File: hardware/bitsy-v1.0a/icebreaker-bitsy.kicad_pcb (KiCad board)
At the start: 4 copper layers, 35.6 x 17.8 mm, 93 parts, among them J1 3V3, J10 4, J11 1, J12 5, J13 7, J14 6, J15 16, J16 15, J17 18, J18 17, J19 19, J2 3V3, J20 20, J21 21, J22 22, J23 23, J24 8, J25 9, J26 13, J27 14, J28 12, J29 11, J3 VIN, J30 10, J31 CDONE, J32 CRESET, J33 USB_C, J34 PROG, J4 GND, J5 GND, J6 GND, J7 2, J8 3, J9 0, P1 UP, P2 UP, P3 UP, P4 UP, SW1 TACT, U1 USBLC6-2, U2 TLV75512PDRV, U3 TLV75533PDRV, U4 LY68L6400, U5 W25Q, U6 ICE40UP5K-SG48, X1 12MHz

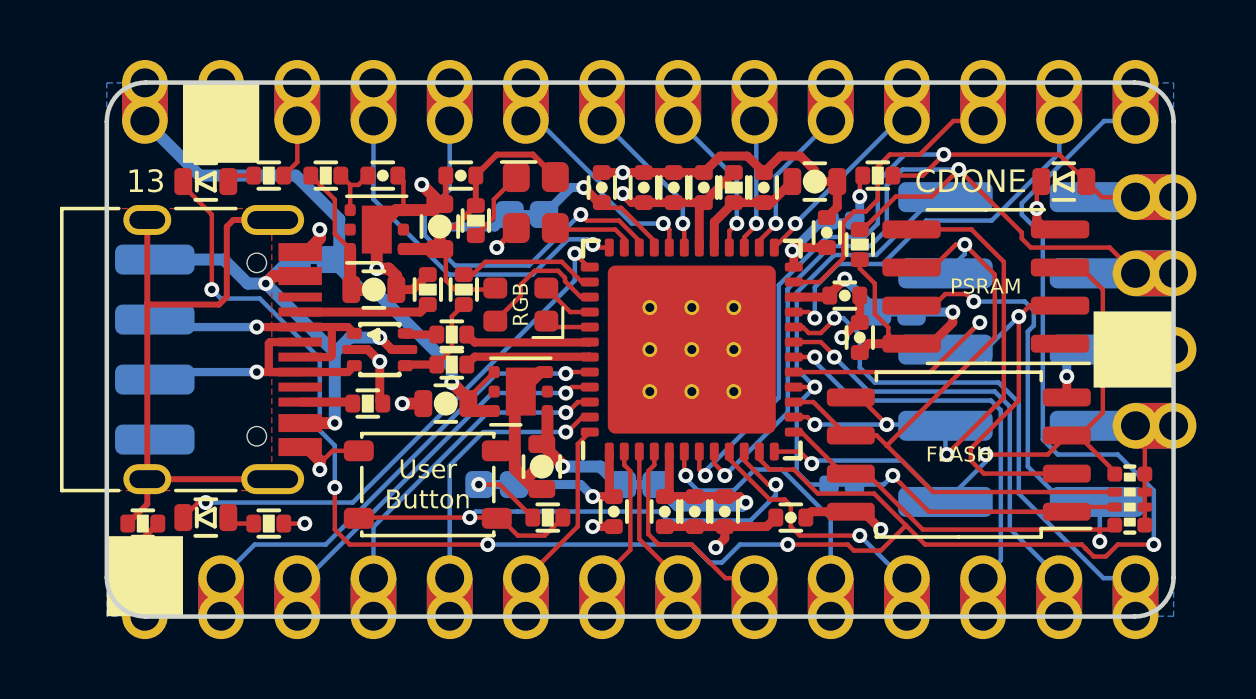
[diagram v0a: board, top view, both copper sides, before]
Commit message: Finish routing bitsy-v1.0a
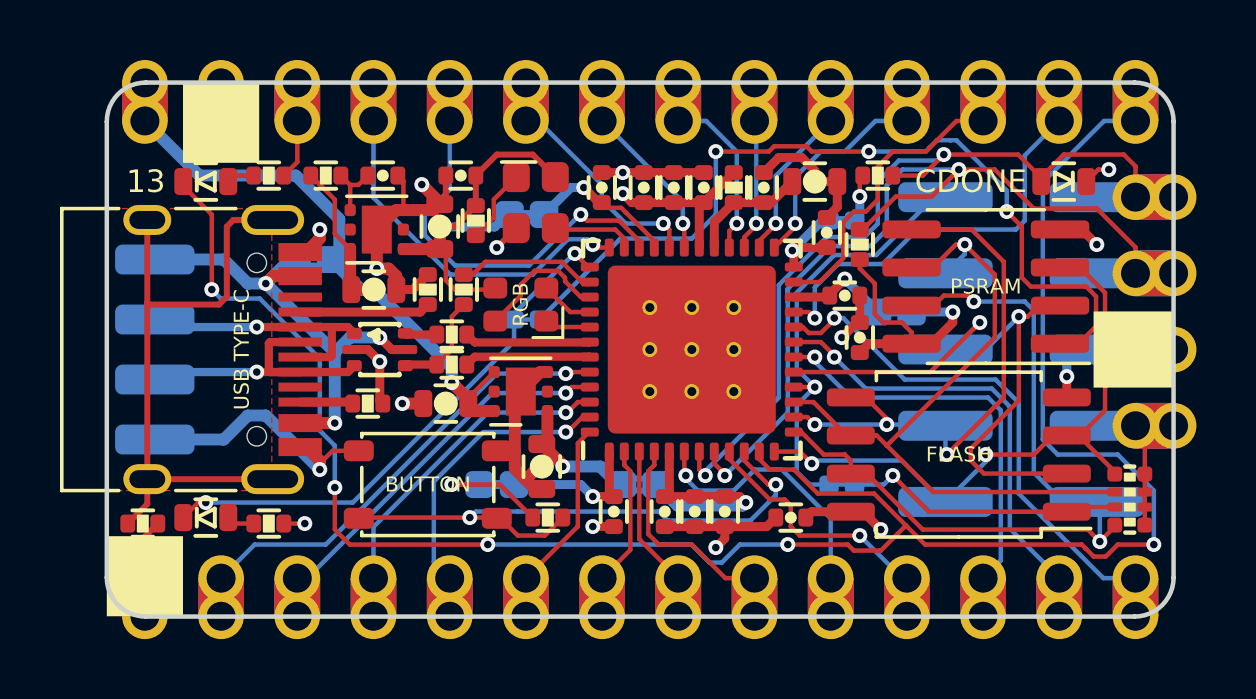
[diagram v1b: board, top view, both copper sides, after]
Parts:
- added JP2: Jumper, pkl_jumpers:J_NC_0402_15, B.Cu at (44.0, 46.5)
- C9: value DNP -> 100n
- JP1: footprint pkl_jumpers:J_NC_0603_30 -> pkl_jumpers:J_NC_0603_20x2
- JP4: renamed from JP3; footprint pkl_jumpers:J_NC_0402_15 -> pkl_jumpers:J_NC_0402_30
- JP5: renamed from JP4; footprint pkl_jumpers:J_NC_0603_30 -> pkl_jumpers:J_NC_0603_20x2
- LOGO1: footprint pkl_logos:null_Logo_SilkS_6.5mm -> pkl_logos:1b2_Logo_SilkS_6.5mm
- turned D3 to 180 degrees
- renumbered JP2 to JP3, JP5 to JP6, JP6 to JP7, JP7 to JP8
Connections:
- net /IOB_20A-~LEDR renamed /~LEDR
- D2 pad C: /RAM_SS-~LEDG -> /~LEDG
- U4 pad 1: /RAM_SS-~LEDG -> /RAM_SS
- U6 pad 37: /RAM_SS-~LEDG -> /~LEDG
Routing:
- net /RAM_SS: track 0.00 -> 28.4 mm, vias 0 -> 3
- net /~LEDG: track 0.00 -> 18.0 mm, vias 0 -> 2
- net /RAM_SS-~LEDG: track 17.9 -> 0.00 mm, vias 2 -> 0
- net GND: track 47.8 -> 52.0 mm, vias 15 -> 16
- net +3V3: track 34.8 -> 36.7 mm
- net /iCE_CDONE: track 25.3 -> 26.8 mm
- net /IOT_36B: track 6.23 -> 7.13 mm
- net /IOB_25B_G3: track 17.7 -> 17.1 mm
- net /IOB_23B: track 12.9 -> 13.5 mm
- net /~LEDR: track 68.8 -> 68.3 mm
- net /IOT_41A: track 5.13 -> 5.68 mm
- removed copper zone on B.Cu, net GND
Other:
- board text added: "1BitSquared"
- board text added: "BUTTON"
- board text added: "CDON"
- board text added: "CRST"
- board text added: "Flsh SS"
- board text added: "RAM SS"
- board text added: "USB"
- board text added: "USB TYPE-C"
- board text added: "Vcc IO0"
- board text added: "Vcc IO1"
- board text added: "Vcc IO2"
- board text removed: "1v2"
- board text removed: "Cdone"
- board text removed: "Cres"
- board text removed: "IO0"
- board text removed: "IO1"
- board text removed: "NULL"
- board text removed: "User Button"
- board text removed: "VBUS"
